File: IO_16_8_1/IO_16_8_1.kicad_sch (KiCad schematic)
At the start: 81 parts, among them J1 Conn_01x06, J2 nmount JST 1mm QWIIC, J3 nmount SW Debug, J4 USB_C_Receptacle_USB2.0, J5 Conn_01x06, SW1 Reset, SW2 Boot, SW3 ADDRESS, U1 ADM3483, U2 W25Q128JVSIQ, U3 RP2040, U4 LMV321, U5 SN74AHCT1G125, U6 AP2112K-3.3, Y1 12MHz,18pF

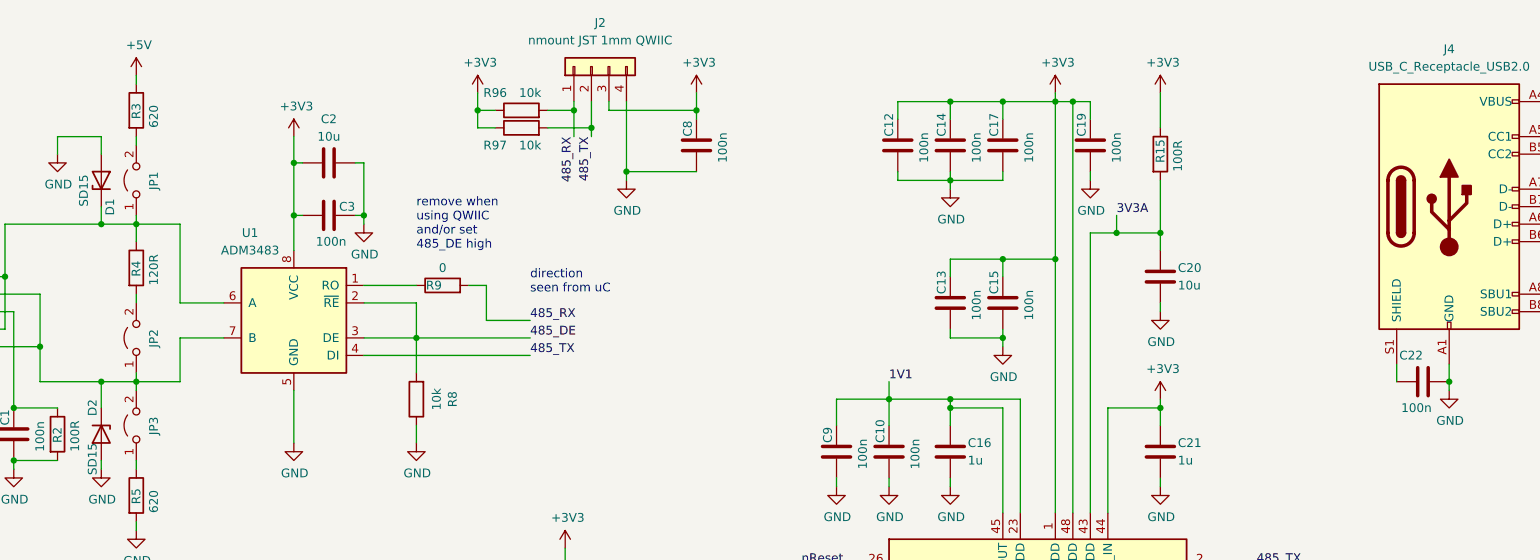
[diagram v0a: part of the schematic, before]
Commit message: upgraed to KiCAD 10.0 and removed the QWIIC support
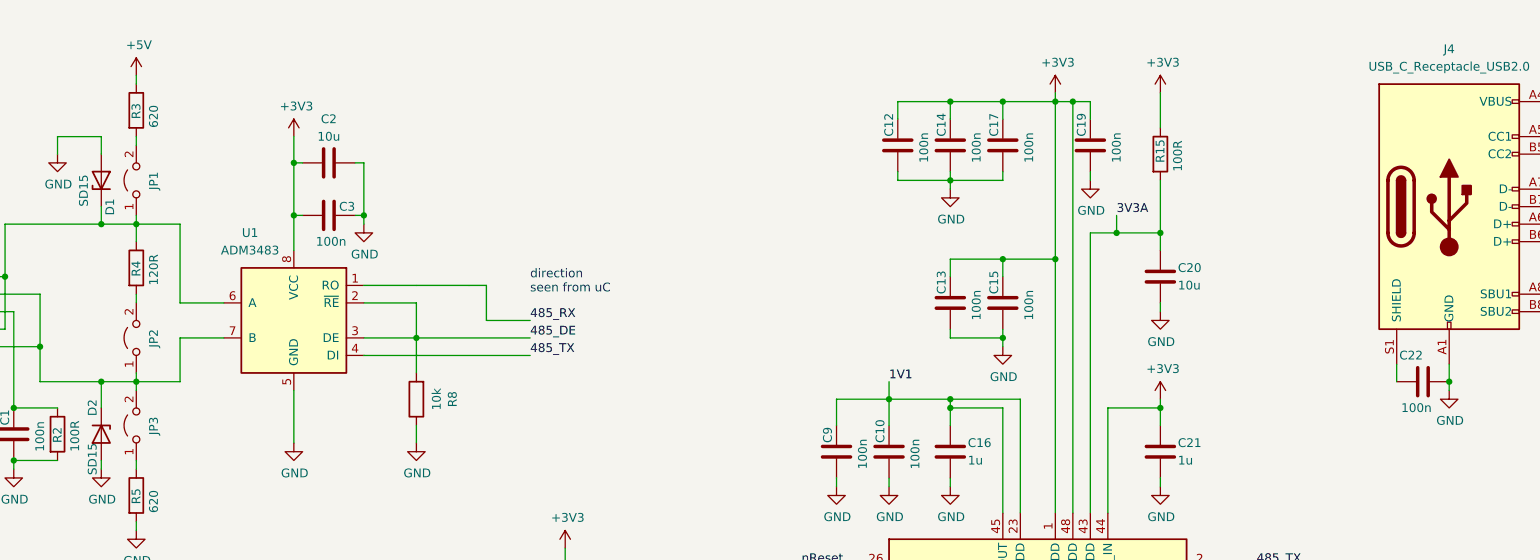
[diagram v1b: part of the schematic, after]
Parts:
- removed C8: 100n, Capacitor_SMD:C_0402_1005Metric, symbol Device:C
- removed J2: nmount JST 1mm QWIIC, Connector_JST:JST_SH_SM04B-SRSS-TB_1x04-1MP_P1.00mm_Horizontal, symbol Connector_Generic:Conn_01x04
- removed R9: 0, Resistor_SMD:R_0603_1608Metric, symbol Device:R
- removed R96, R97: 10k, Resistor_SMD:R_0603_1608Metric, symbol Device:R
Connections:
- net 485_RX: now also U1.1 (RO)
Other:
- note removed: "remove when using QWIIC and/or set 485_DE high"
